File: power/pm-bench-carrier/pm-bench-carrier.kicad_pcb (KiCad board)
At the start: 2 copper layers, 130 x 55 mm, 52 parts, among them J1 VIN 40-60V, J2 VOUT 19V, Q1 2N7002

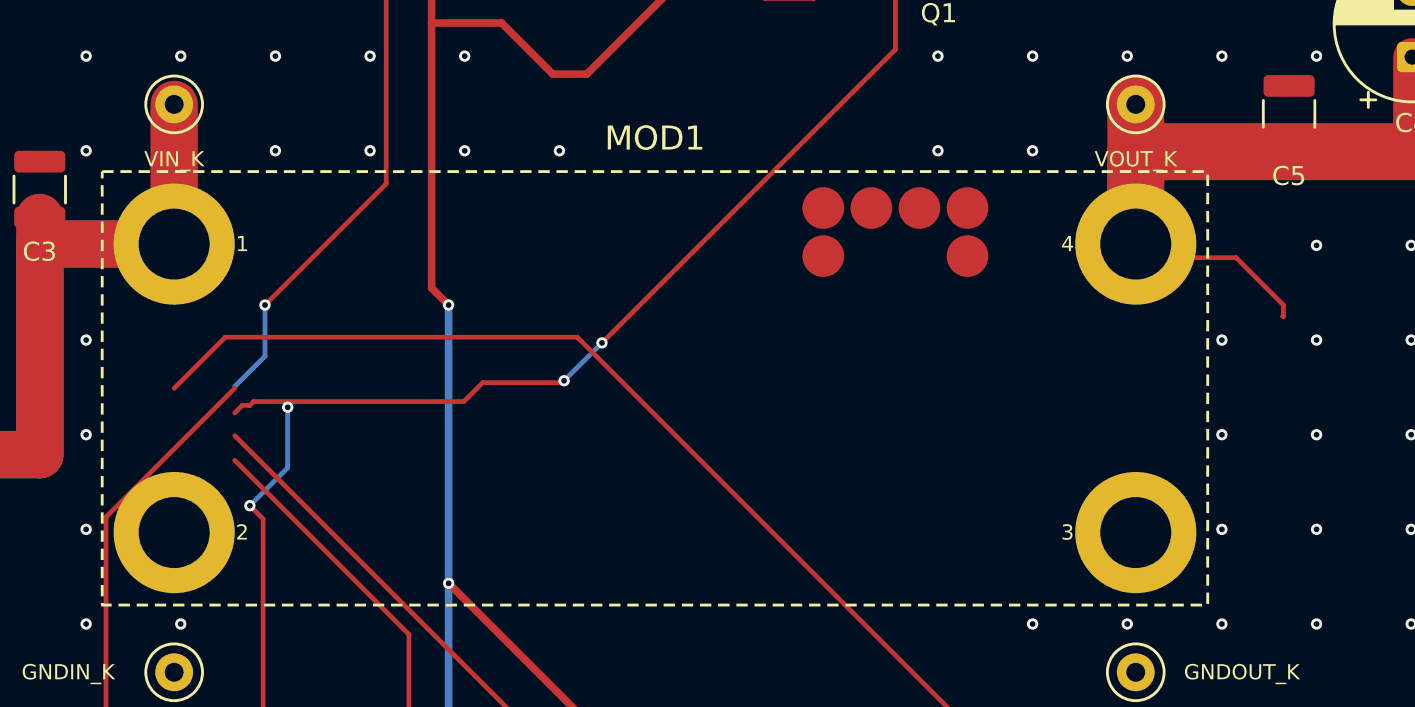
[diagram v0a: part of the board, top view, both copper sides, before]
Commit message: Revert "power: screwed PM module mount footprints (M2 into SMT standoffs, pogo aux) on module, plane and bench carrier; RUN moves to aux pad 8; copper not yet rerouted"
This reverts commit abb9f50ba34d0b63e5425fa3cd376420f2890e7d.
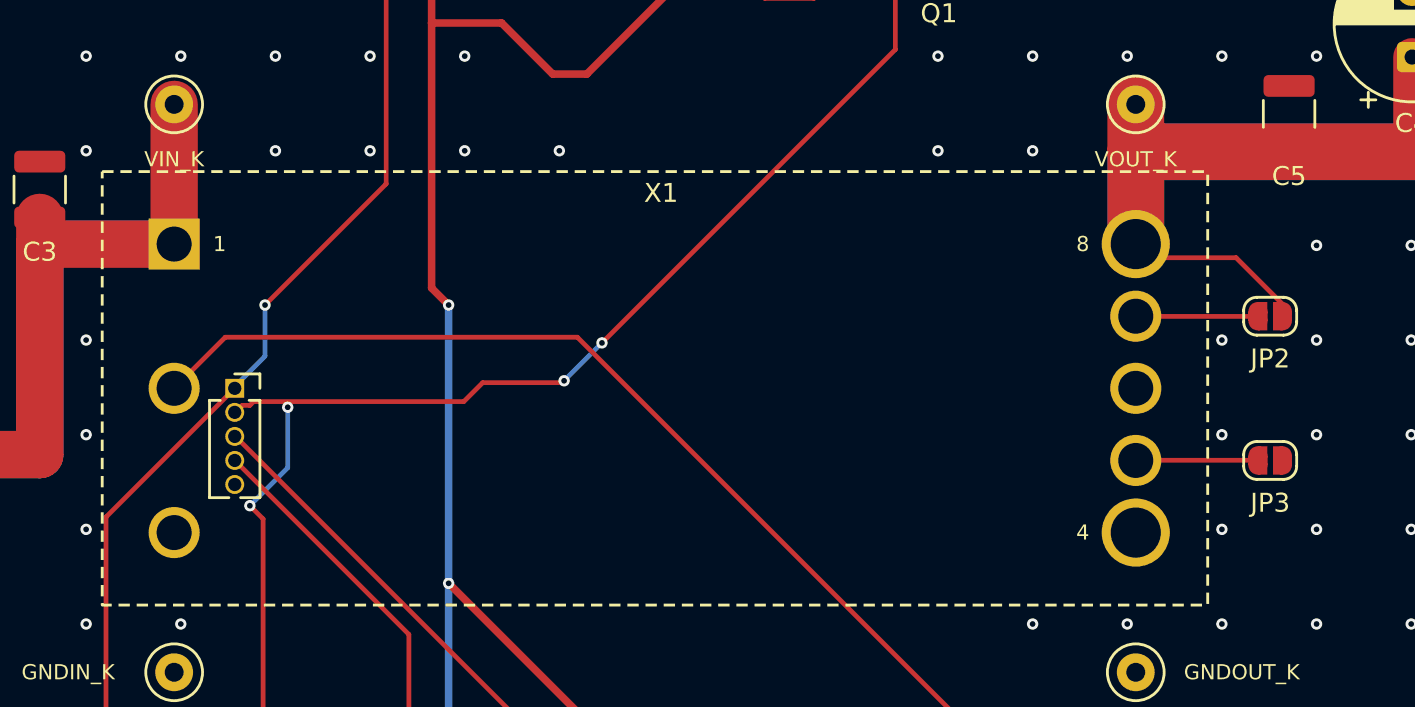
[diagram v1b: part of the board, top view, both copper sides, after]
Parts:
- removed MOD1: PM_Module_Outline, carrier:PM_Module_Outline
- removed PG1, PG2, PG3, PG4, PG5, PG8: pogo, carrier:PM_Pogo_YZ130115073P
- removed SO1, SO2, SO3, SO4: M2x6 standoff, carrier:PM_Standoff_M2x6_SMTSO
- added JP2: SENSE+, Jumper:SolderJumper-2_P1.3mm_Open_RoundedPad1.0x1.5mm, F.Cu at (197.5, 123.7)
- added JP3: SENSE-, Jumper:SolderJumper-2_P1.3mm_Open_RoundedPad1.0x1.5mm, F.Cu at (197.5, 131.3)
- added X1: PM-19V-200W, carrier:Brick_Eighth_DOSA_Socket, F.Cu at (165.0, 127.5)
- added X2: Aux socket, Connector_PinSocket_1.27mm:PinSocket_1x05_P1.27mm_Vertical, F.Cu at (142.8, 127.5)
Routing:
- net Net-(JP3-A): track 0.00 -> 6.00 mm
- net Net-(JP2-A): track 0.00 -> 6.00 mm

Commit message: power: screwed PM module mount footprints (M2 into SMT standoffs, pogo aux) on module, plane and bench carrier; RUN moves to aux pad 8; copper not yet rerouted
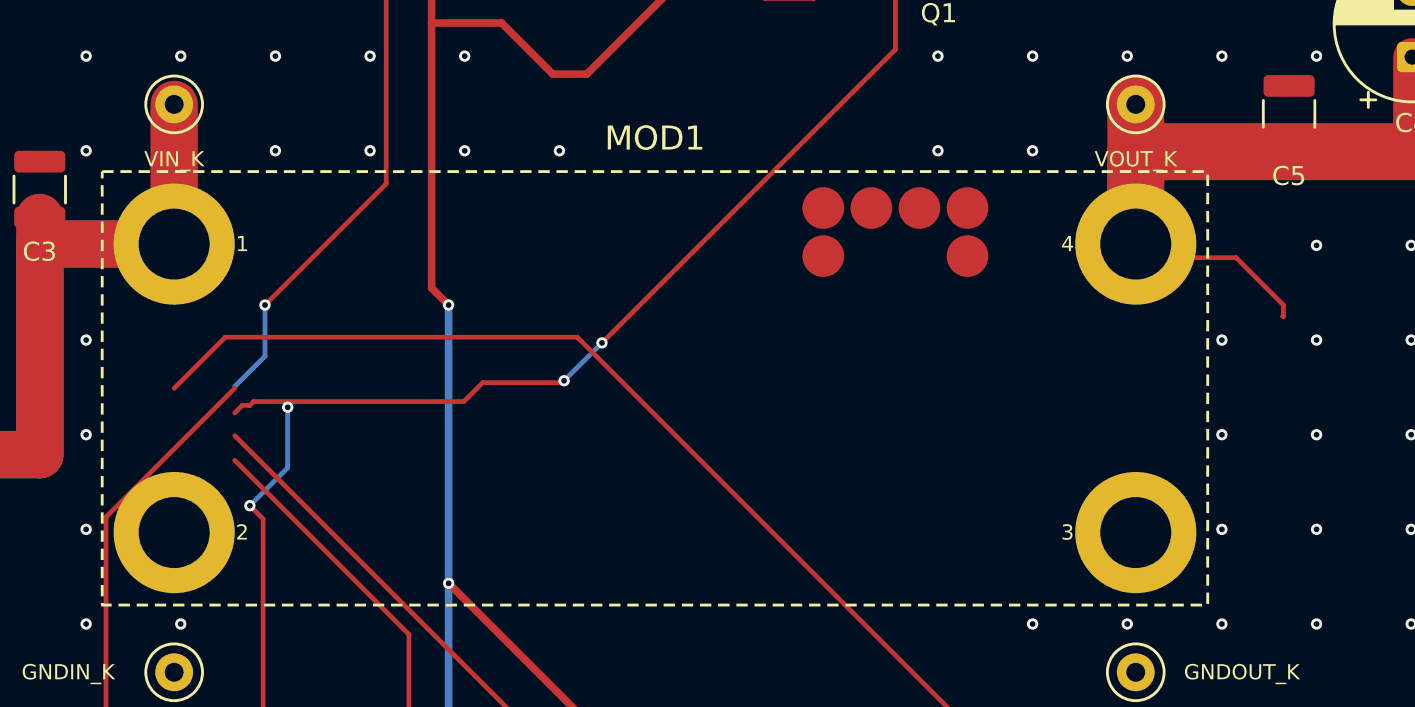
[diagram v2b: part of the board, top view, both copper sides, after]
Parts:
- removed JP2: SENSE+, Jumper:SolderJumper-2_P1.3mm_Open_RoundedPad1.0x1.5mm
- removed JP3: SENSE-, Jumper:SolderJumper-2_P1.3mm_Open_RoundedPad1.0x1.5mm
- removed X1: PM-19V-200W, carrier:Brick_Eighth_DOSA_Socket
- removed X2: Aux socket, Connector_PinSocket_1.27mm:PinSocket_1x05_P1.27mm_Vertical
- added MOD1: PM_Module_Outline, carrier:PM_Module_Outline, F.Cu at (165.0, 127.5)
- added PG1: pogo, carrier:PM_Pogo_YZ130115073P, F.Cu at (173.9, 118.0)
- added PG2: pogo, carrier:PM_Pogo_YZ130115073P, F.Cu at (176.4, 118.0)
- added PG3: pogo, carrier:PM_Pogo_YZ130115073P, F.Cu at (179.0, 118.0)
- added PG4: pogo, carrier:PM_Pogo_YZ130115073P, F.Cu at (181.5, 118.0)
- added PG5: pogo, carrier:PM_Pogo_YZ130115073P, F.Cu at (173.9, 120.5)
- added PG8: pogo, carrier:PM_Pogo_YZ130115073P, F.Cu at (181.5, 120.5)
- added SO1: M2x6 standoff, carrier:PM_Standoff_M2x6_SMTSO, F.Cu at (139.6, 119.9)
- added SO2: M2x6 standoff, carrier:PM_Standoff_M2x6_SMTSO, F.Cu at (139.6, 135.1)
- added SO3: M2x6 standoff, carrier:PM_Standoff_M2x6_SMTSO, F.Cu at (190.4, 135.1)
- added SO4: M2x6 standoff, carrier:PM_Standoff_M2x6_SMTSO, F.Cu at (190.4, 119.9)
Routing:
- net Net-(JP3-A): track 6.00 -> 0.00 mm
- net Net-(JP2-A): track 6.00 -> 0.00 mm
